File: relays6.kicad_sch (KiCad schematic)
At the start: 24 parts, among them K11 Fujitsu_FTR-LYAA005x, K12 Fujitsu_FTR-LYAA005x, K14 Fujitsu_FTR-LYAA005x, K16 Fujitsu_FTR-LYAA005x, K18 Fujitsu_FTR-LYAA005x, K20 Fujitsu_FTR-LYAA005x, Q867 2N7002, Q868 2N7002, Q870 2N7002, Q872 2N7002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

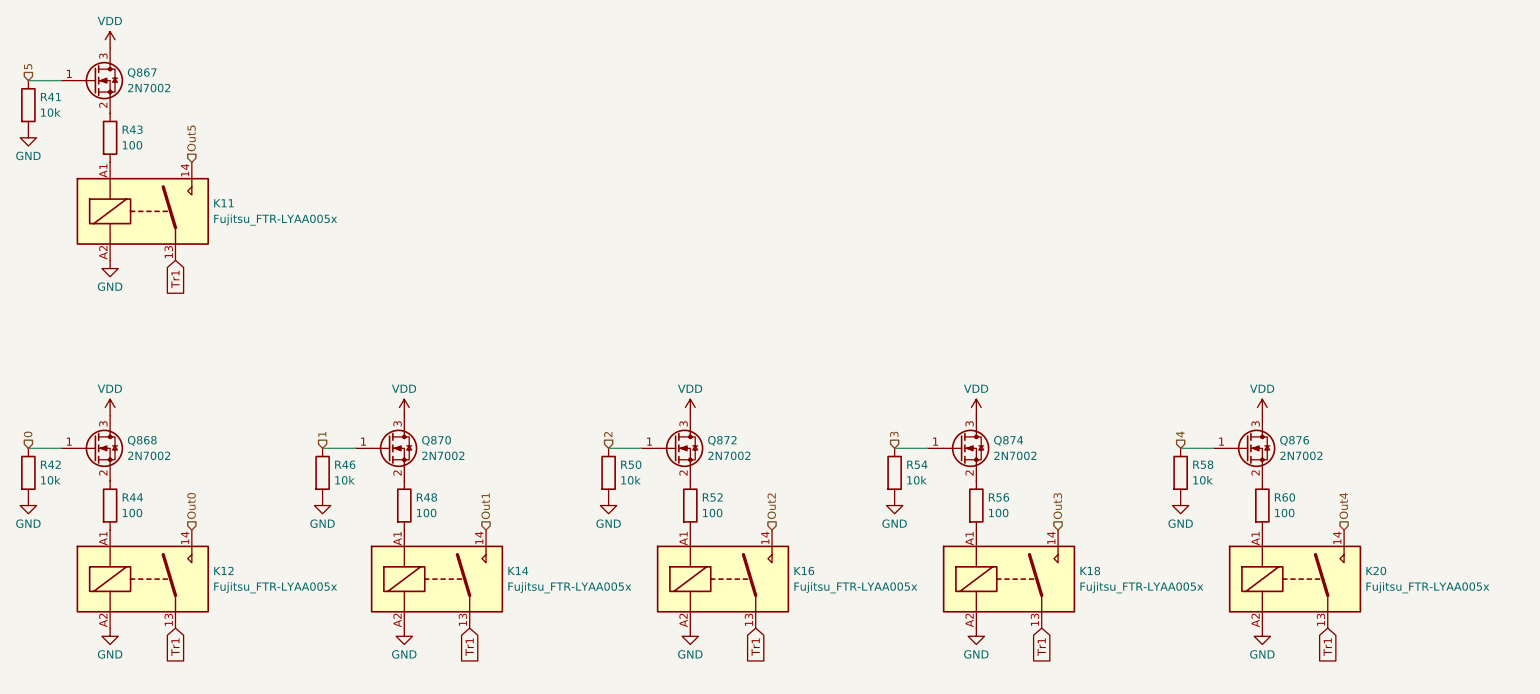
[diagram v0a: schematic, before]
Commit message: moved to 3v3
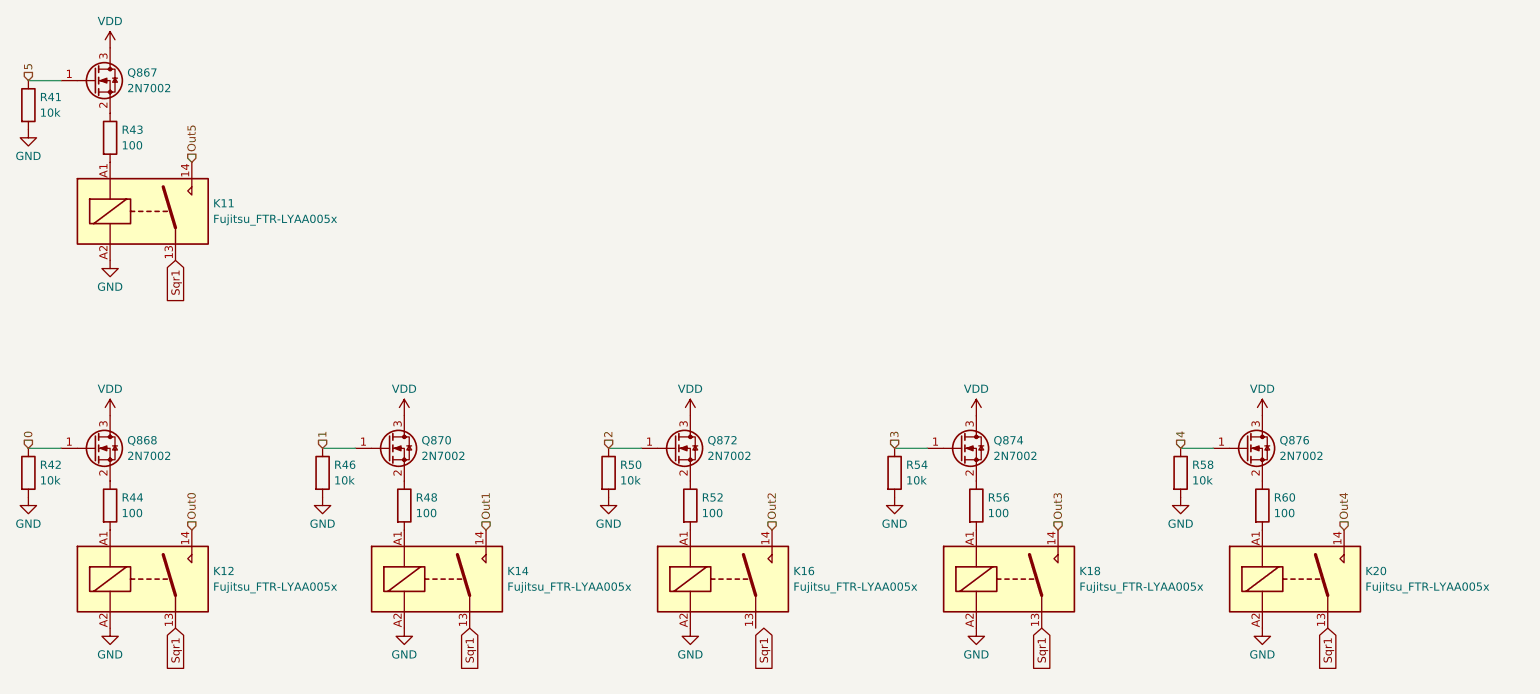
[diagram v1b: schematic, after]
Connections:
- net Tr1 renamed Sqr1
- net Sqr1: no longer K16.13
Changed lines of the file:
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@@
 		)
 	)
-	(global_label "Tr1"
+	(global_label "Sqr1"
+		(shape input)
+		(at 105.41 132.08 270)
+		(fields_autoplaced yes)
+		(effects
+			(font
+				(size 1.27 1.27)
+			)
+			(justify right)
+		)
+		(property "Intersheetrefs" "${INTERSHEET_REFS}"
+			(at 105.41 139.4194 90)
+			(effects
+				(font
+					(size 1.27 1.27)
+				)
+				(justify right)
+				(hide yes)
+			)
+		)
+	)
+	(global_label "Sqr1"
+		(shape input)
+		(at 238.76 132.08 270)
+		(fields_autoplaced yes)
+		(effects
+			(font
+				(size 1.27 1.27)
+			)
+			(justify right)
+		)
+		(property "Intersheetrefs" "${INTERSHEET_REFS}"
+			(at 238.76 139.4194 90)
+			(effects
+				(font
+					(size 1.27 1.27)
+				)
+				(justify right)
+				(hide yes)
+			)
+		)
+	)
+	(global_label "Sqr1"
 		(shape input)
 		(at 59.69 74.93 270)
@@
 		)
 		(property "Intersheetrefs" "${INTERSHEET_REFS}"
-			(at 59.69 80.8785 90)
+			(at 59.69 82.2694 90)
 			(effects
 				(font
@@
 		)
 	)
-	(global_label "Tr1"
+	(global_label "Sqr1"
 		(shape input)
-		(at 105.41 132.08 270)
+		(at 151.13 132.08 270)
 		(fields_autoplaced yes)
 		(effects
@@
 		)
 		(property "Intersheetrefs" "${INTERSHEET_REFS}"
-			(at 105.41 138.0285 90)
+			(at 151.13 139.4194 90)
 			(effects
 				(font
@@
 		)
 	)
-	(global_label "Tr1"
+	(global_label "Sqr1"
 		(shape input)
-		(at 149.86 132.08 270)
+		(at 59.69 132.08 270)
 		(fields_autoplaced yes)
 		(effects
@@
 		)
 		(property "Intersheetrefs" "${INTERSHEET_REFS}"
-			(at 149.86 138.0285 90)
+			(at 59.69 139.4194 90)
 			(effects
 				(font
@@
 		)
 	)
-	(global_label "Tr1"
+	(global_label "Sqr1"
 		(shape input)
 		(at 194.31 132.08 270)
@@
 		)
 		(property "Intersheetrefs" "${INTERSHEET_REFS}"
-			(at 194.31 138.0285 90)
+			(at 194.31 139.4194 90)
 			(effects
 				(font
-					(size 1.27 1.27)
-				)
-				(justify right)
-				(hide yes)
-			)
-		)
-	)
-	(global_label "Tr1"
-		(shape input)
-		(at 238.76 132.08 270)
-		(fields_autoplaced yes)
-		(effects
-			(font
-				(size 1.27 1.27)
-			)
-			(justify right)
-		)
-		(property "Intersheetrefs" "${INTERSHEET_REFS}"
-			(at 238.76 138.0285 90)
-			(effects
-				(font
-					(size 1.27 1.27)
-				)
-				(justify right)
-				(hide yes)
-			)
-		)
-	)
-	(global_label "Tr1"
-		(shape input)
-		(at 59.69 132.08 270)
-		(fields_autoplaced yes)
-		(effects
-			(font
-				(size 1.27 1.27)
-			)
-			(justify right)
-		)
-		(property "Intersheetrefs" "${INTERSHEET_REFS}"
-			(at 59.69 138.0285 90)
-			(effects
-				(font

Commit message: added decoupling caps
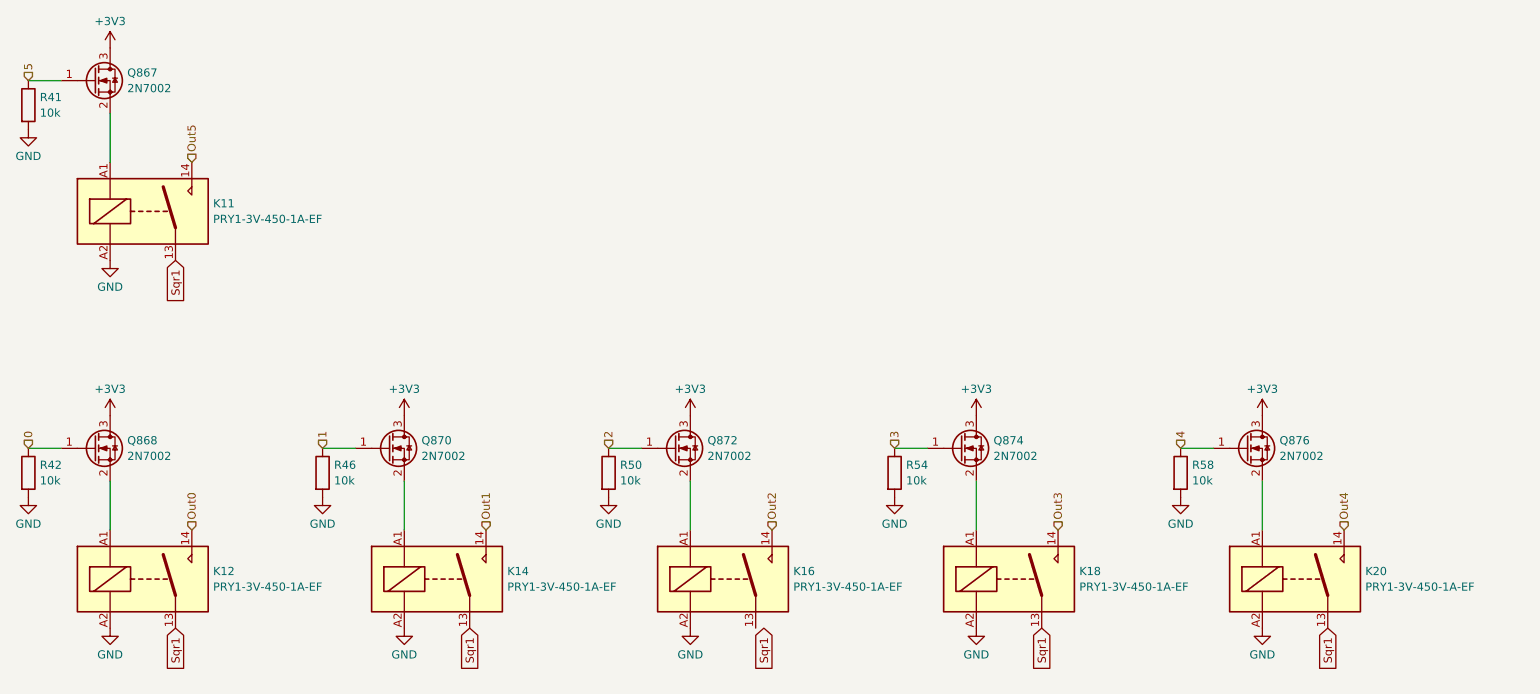
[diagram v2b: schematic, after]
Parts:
- removed R43, R44, R48, R52, R56, R60: 100, Resistor_SMD:R_0402_1005Metric, symbol Device:R
- K11, K12, K14, K16, K18, K20: value Fujitsu_FTR-LYAA005x -> PRY1-3V-450-1A-EF
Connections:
- net at Q867.2 (S): now also K11.A1
- net at Q868.2 (S): now also K12.A1
- net at K14.A1: now also Q870.2 (S)
- net at K20.A1: now also Q876.2 (S)
- net at K18.A1: now also Q874.2 (S)
- net at K16.A1: now also Q872.2 (S)
- net VDD renamed +3V3

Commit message: corrected output/input type of pins
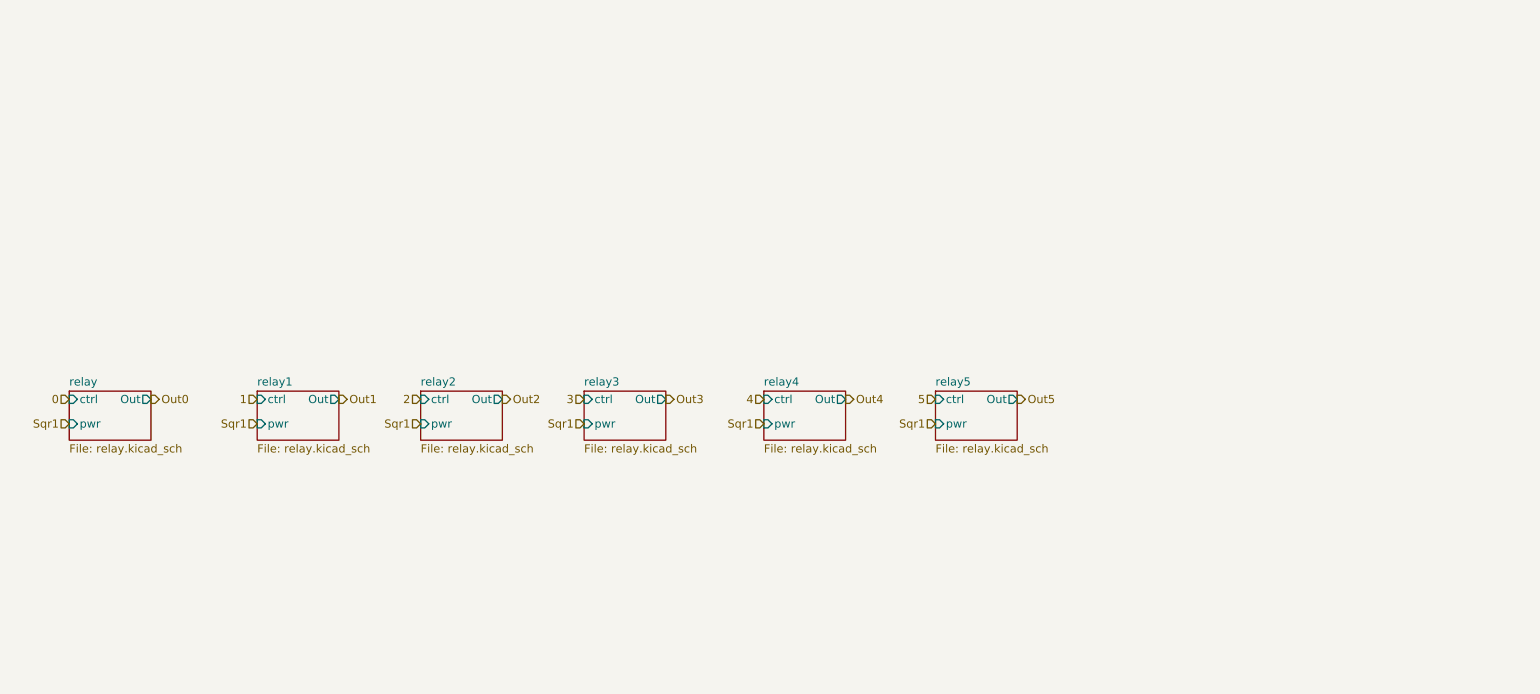
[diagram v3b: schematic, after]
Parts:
- removed K11, K12, K14, K16, K18, K20: PRY1-3V-450-1A-EF, Relay_THT:Relay_SPST-NO_Fujitsu_FTR-LYAA005x_FormA_Vertical, symbol Relay:Fujitsu_FTR-LYAA005x
- removed Q867, Q868, Q870, Q872, Q874, Q876: 2N7002, Package_TO_SOT_SMD:SOT-23, symbol Transistor_FET:2N7002
- removed R41, R42, R46, R50, R54, R58: 10k, Resistor_SMD:R_0402_1005Metric, symbol Device:R
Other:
- added sheet relay (relay.kicad_sch)
- added sheet relay1 (relay.kicad_sch)
- added sheet relay2 (relay.kicad_sch)
- added sheet relay3 (relay.kicad_sch)
- added sheet relay4 (relay.kicad_sch)
- added sheet relay5 (relay.kicad_sch)

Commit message: schematic cleanup, routed 1 bdc
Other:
- removed sheet relay
- removed sheet relay1
- removed sheet relay2
- removed sheet relay3
- removed sheet relay4
- removed sheet relay5
- added sheet SSR (ssr.kicad_sch)
- added sheet SSR1 (ssr.kicad_sch)
- added sheet SSR2 (ssr.kicad_sch)
- added sheet SSR3 (ssr.kicad_sch)
- added sheet SSR4 (ssr.kicad_sch)
- added sheet SSR5 (ssr.kicad_sch)

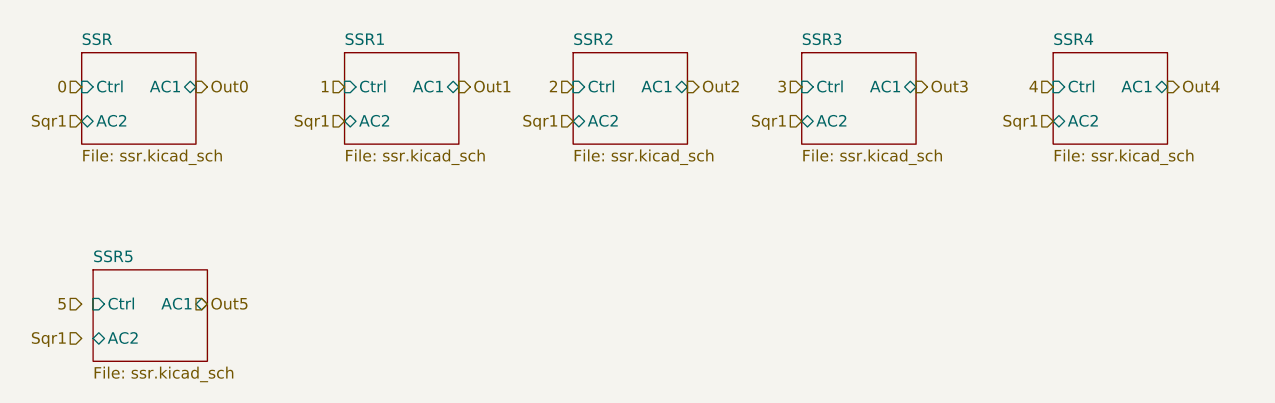
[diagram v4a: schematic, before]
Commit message: switched to using SSR module
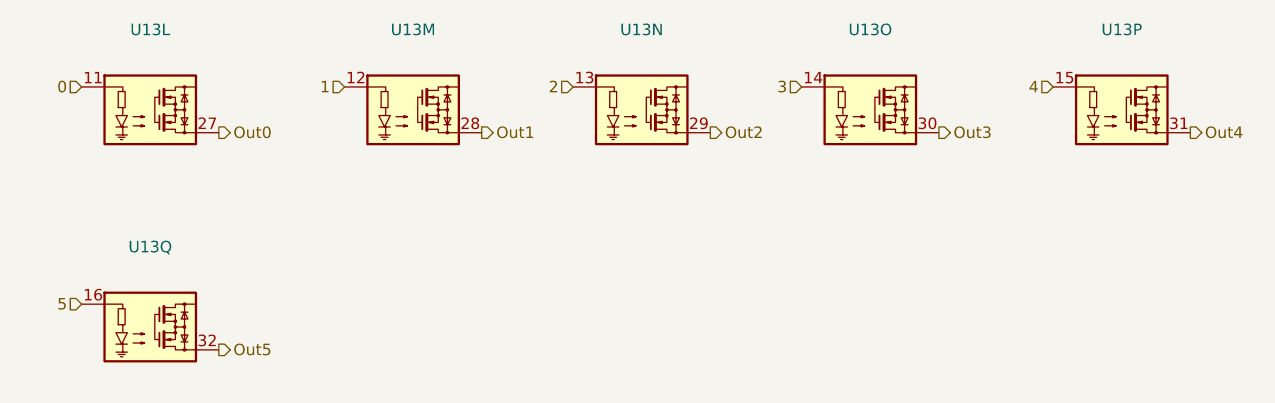
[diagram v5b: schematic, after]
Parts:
- added U13: ~, symbol custom:SSR
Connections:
- net 0: now also U13.11
- net 1: now also U13.12
- net 2: now also U13.13
- net 3: now also U13.14
- net 4: now also U13.15
- net 5: now also U13.16
- net Out0: now also U13.27
- net Out1: now also U13.28
- net Out2: now also U13.29
- net Out3: now also U13.30
- net Out4: now also U13.31
- net Out5: now also U13.32
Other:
- removed sheet SSR
- removed sheet SSR1
- removed sheet SSR2
- removed sheet SSR3
- removed sheet SSR4
- removed sheet SSR5
